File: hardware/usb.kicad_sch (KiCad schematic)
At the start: 35 parts, among them J1 USB_A_Stacked, J2 USB_C_Receptacle_USB2.0_14P, J3 USB_C_Receptacle_USB2.0_14P, J4 USB_C_Receptacle_USB2.0_14P, U10 SY6280AAC, U11 SY6280AAC, U12 SY6280AAC, U13 TPD2EUSB30, U14 TPD2EUSB30, U15 TPD2EUSB30, U16 TPD2EUSB30, U17 HUSB237, U18 TPD2EUSB30, U9 SY6280AAC

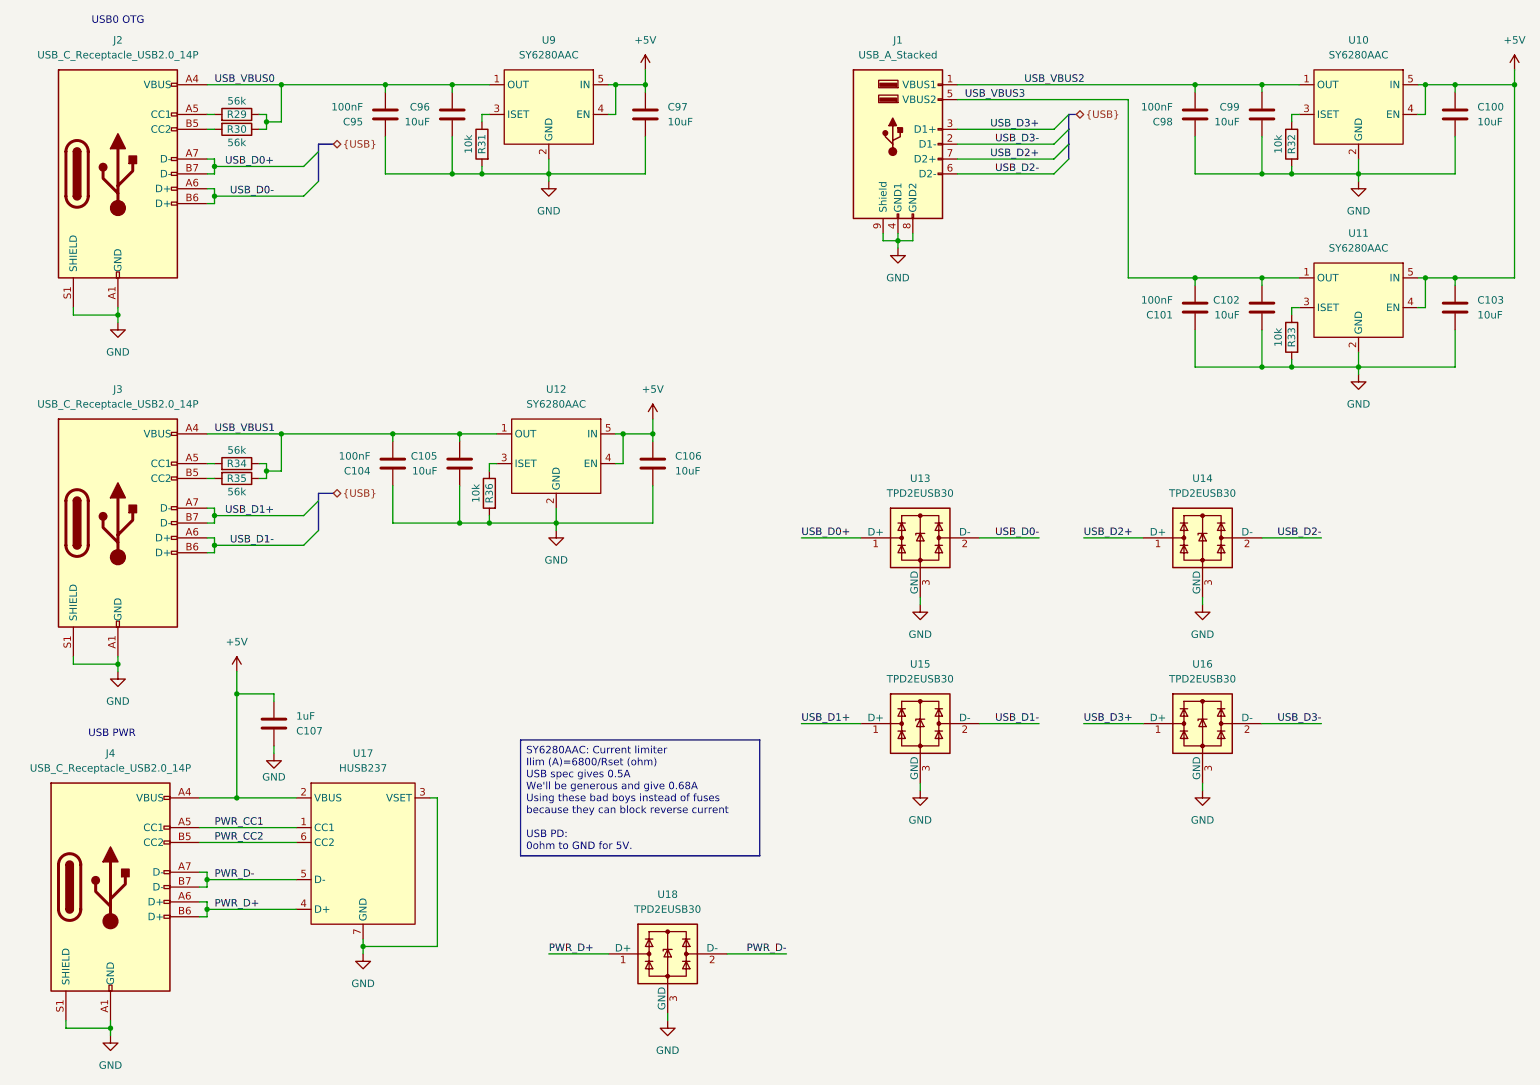
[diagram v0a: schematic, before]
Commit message: Improve routing and add test pads
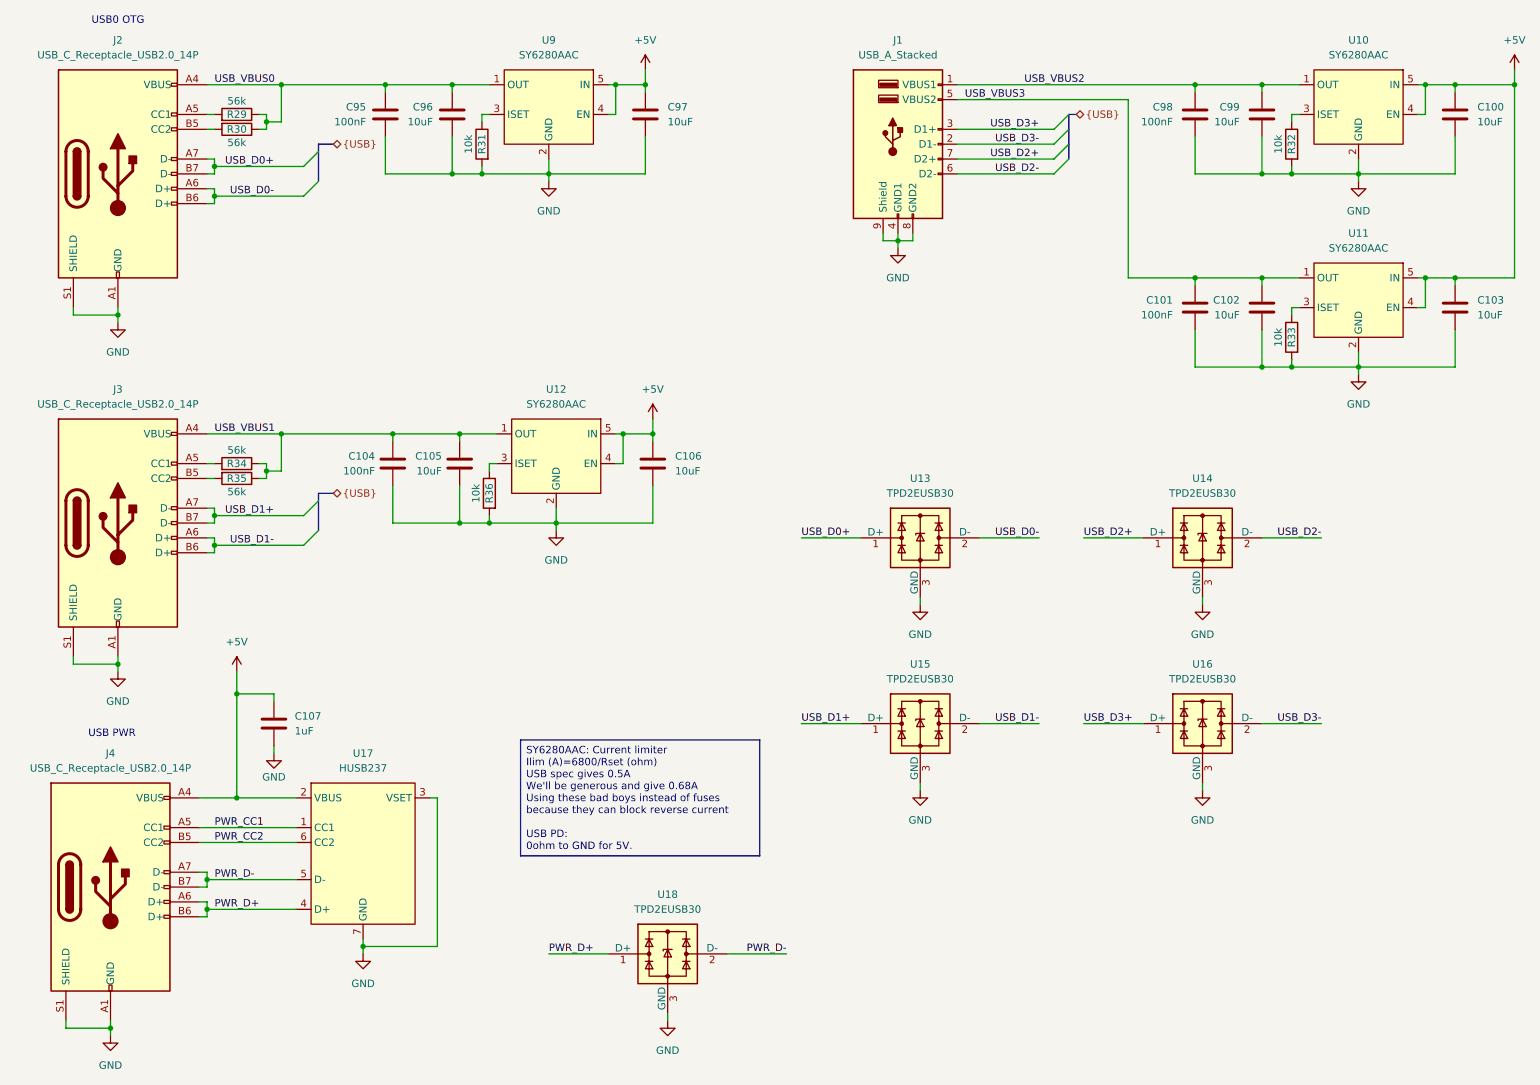
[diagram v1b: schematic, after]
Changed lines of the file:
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@@
 		(dnp no)
 		(property "Reference" "C107"
-			(at 73.66 137.1601 0)
+			(at 73.406 134.62 0)
 			(effects
 				(font
@@
 		)
 		(property "Value" "1uF"
-			(at 73.66 134.6201 0)
+			(at 73.406 137.1601 0)
 			(effects
 				(font
@@
 		(dnp no)
 		(property "Reference" "C96"
-			(at 96.52 30.4799 0)
+			(at 97.028 30.4798 0)
 			(effects
 				(font
@@
 		)
 		(property "Value" "10uF"
-			(at 96.52 33.0199 0)
+			(at 97.028 33.0198 0)
 			(effects
 				(font
@@
 		(dnp no)
 		(property "Reference" "C105"
-			(at 97.79 90.1699 0)
+			(at 98.552 90.17 0)
 			(effects
 				(font
@@
 		)
 		(property "Value" "10uF"
-			(at 97.79 92.7099 0)
+			(at 98.552 92.71 0)
 			(effects
 				(font
@@
 		(dnp no)
 		(property "Reference" "C104"
-			(at 86.36 92.7101 0)
+			(at 87.122 90.1701 0)
 			(effects
 				(font
@@
 		)
 		(property "Value" "100nF"
-			(at 86.36 90.1701 0)
+			(at 87.122 92.7101 0)
 			(effects
 				(font
@@
 		(dnp no)
 		(property "Reference" "C101"
-			(at 223.52 66.0401 0)
+			(at 223.52 63.5001 0)
 			(effects
 				(font
@@
 		)
 		(property "Value" "100nF"
-			(at 223.52 63.5001 0)
+			(at 223.52 66.04 0)
 			(effects
 				(font
@@
 		(dnp no)
 		(property "Reference" "C95"
-			(at 85.09 33.0201 0)
+			(at 85.598 30.48 0)
 			(effects
 				(font
@@
 		)
 		(property "Value" "100nF"
-			(at 85.09 30.4801 0)
+			(at 85.598 33.0199 0)
 			(effects
 				(font
@@
 		(dnp no)
 		(property "Reference" "C98"
-			(at 223.52 33.0201 0)
+			(at 223.52 30.4801 0)
 			(effects
 				(font
@@
 		)
 		(property "Value" "100nF"
-			(at 223.52 30.4801 0)
-			(effects
-				(font
+			(at 223.52 33.02 0)
+			(effects
+				(font
